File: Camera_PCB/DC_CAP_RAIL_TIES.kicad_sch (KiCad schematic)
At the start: 31 parts

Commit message: cleaned up Camera_PCB \repository
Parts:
- removed R11: 240, symbol Device:R
- added C75, C76, C77, C78, C79: 0.1u, Capacitor_SMD:C_0603_1608Metric_Pad1.08x0.95mm_HandSolder, symbol Device:C
- added R11: 240, Resistor_SMD:R_0603_1608Metric_Pad0.98x0.95mm_HandSolder, symbol Device:R_US
- added R30: 200k 1%, Resistor_SMD:R_0603_1608Metric_Pad0.98x0.95mm_HandSolder, symbol Device:R_Small_US
- C10: value 0.1u -> 1u; DPN (none) -> GCM188R71E105KA64D; Distributor (none) -> DigiKey; now not fitted
- C11, C12, C13, C14, C15, C16, C17, C18, C22, C23, C28, C29, C32, C33: DPN (none) -> GRM188R72A104KA35D; Distributor (none) -> DigiKey
- C19, C25, C30, C7: DPN (none) -> GRM21BZ71E106KE15L; Distributor (none) -> DigiKey
- C20, C26, C27, C31, C8, C9: footprint Capacitor_SMD:C_0805_2012Metric_Pad1.18x1.45mm_HandSolder -> Capacitor_SMD:C_0603_1608Metric_Pad1.08x0.95mm_HandSolder; DPN (none) -> GCM188R71E105KA64D; Distributor (none) -> DigiKey
- C21: footprint Capacitor_SMD:C_0805_2012Metric_Pad1.18x1.45mm_HandSolder -> Capacitor_SMD:C_0603_1608Metric_Pad1.08x0.95mm_HandSolder; DPN (none) -> GCM188R71E105KA64D; Distributor (none) -> DigiKey; now not fitted
- C24: DPN (none) -> GRM188R72A104KA35D; Distributor (none) -> DigiKey; now not fitted
- C37: DPN (none) -> GRM21BZ71H475ME15K; Distributor (none) -> DigiKey
- R10, R9: footprint Resistor_SMD:R_0805_2012Metric_Pad1.20x1.40mm_HandSolder -> Resistor_SMD:R_0603_1608Metric_Pad0.98x0.95mm_HandSolder; DPN (none) -> RC0603FR-102KL; Distributor (none) -> DigiKey
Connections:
- net +1V8: now also C75.2, C76.2
- net +3.3V: no longer C16.2
- net GND: now also C75.1, C76.1, C77.1, C78.1, C79.1, R11.2, R30.1
- net SVREF: now also C77.2
- net SZQ: now also R11.1
- new net VCC-RTC: C16.2
- new net VRA1: C79.2
- new net VRA2: C78.2, R30.2
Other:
- note added: "11 DRAM power pins, four physically separate groups of pins"
- note added: "Place close to v3s pin"
- note added: "Use +/-1% for these 2kR"
- note added: "Voltage Notes: 3.3V - VCC-IO, HPVCC, VCC-USB, VCC-EPHY, VCC-MCSI, VCC-PE 3.3V (always on) - VCC-RTC 3.0V - AVCC, VCC-PLL 1.8V - VCC-DRAM 1.2V - VDD-CPU, VDD-SYS UNPOWERED BUT DECOUPLED: VRA1, VRA2"
- note added: "use +/-1% R"
- note removed: "1.2V - VDD-CPU, VDD-SYS"
- note removed: "1.8V - VCC-DRAM"
- note removed: "3.0V - AVCC, VCC-PLL"
- note removed: "3.3V - VCC-IO, HPVCC, VCC-USB, VCC-EPHY, VCC-MCSI, VCC-PE, VCC-RTC"
- note removed: "Voltage Notes"
- moved on the sheet: C12, C13, C14, C15, C16, C17, C18, C19, C20, C22, C23, C37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

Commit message: Thorough Camera PCB Review by Jack
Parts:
- added TP14: SVREF, TestPoint:TestPoint_Pad_D1.5mm, symbol Connector:TestPoint
- added TP15: SZQ, TestPoint:TestPoint_Pad_D1.5mm, symbol Connector:TestPoint
- added TP28, TP29, TP30, TP31, TP32: GND, TestPoint:TestPoint_Pad_D1.5mm, symbol Connector:TestPoint
- R30: value 200k 1% -> 200k
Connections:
- net GND: now also TP28.1, TP29.1, TP30.1, TP31.1, TP32.1
- net SVREF: now also TP14.1
- net SZQ: now also TP15.1
- net +3.3V renamed +3V3
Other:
- note added: "Ground Test Points"
- note added: "Powered Decoupled Lines"
- note added: "Unpowered Decoupled Lines"
- moved on the sheet: C18, C78, R30

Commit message: more schematic changes, added solder bridges, etc
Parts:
- TP14, TP15, TP28, TP29, TP30, TP31, TP32: now left out of the parts list
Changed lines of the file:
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@@
 		(unit 1)
 		(exclude_from_sim no)
-		(in_bom yes)
+		(in_bom no)
 		(on_board yes)
 		(dnp no)
@@
 		(unit 1)
 		(exclude_from_sim no)
-		(in_bom yes)
+		(in_bom no)
 		(on_board yes)
 		(dnp no)
@@
 		(unit 1)
 		(exclude_from_sim no)
-		(in_bom yes)
+		(in_bom no)
 		(on_board yes)
 		(dnp no)
@@
 		(unit 1)
 		(exclude_from_sim no)
-		(in_bom yes)
+		(in_bom no)
 		(on_board yes)
 		(dnp no)
@@
 		(unit 1)
 		(exclude_from_sim no)
-		(in_bom yes)
+		(in_bom no)
 		(on_board yes)
 		(dnp no)
@@
 		(unit 1)
 		(exclude_from_sim no)
-		(in_bom yes)
+		(in_bom no)
 		(on_board yes)
 		(dnp no)
@@
 		(unit 1)
 		(exclude_from_sim no)
-		(in_bom yes)
+		(in_bom no)
 		(on_board yes)
 		(dnp no)

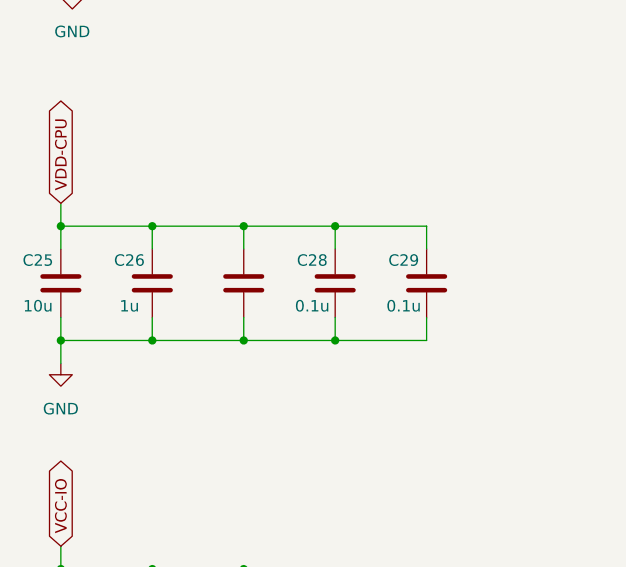
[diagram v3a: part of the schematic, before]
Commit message: PCB commit before reorganizing
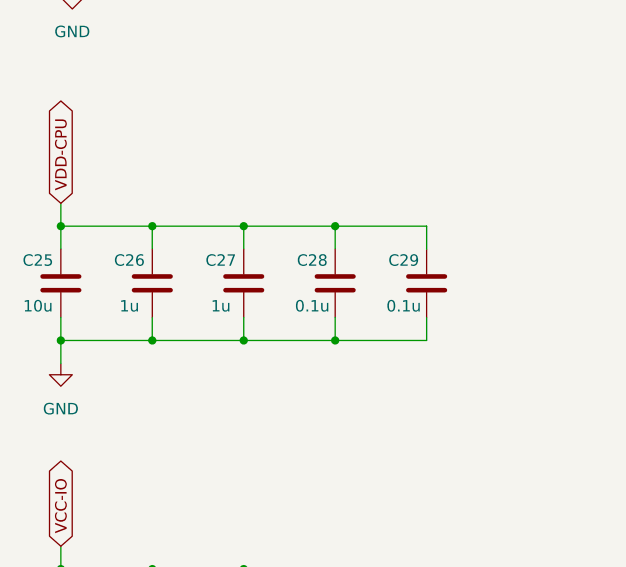
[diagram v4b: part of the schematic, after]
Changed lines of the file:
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@@
 					(size 1.27 1.27)
 				)
-				(hide yes)
 			)
 		)
@@
 					(size 1.27 1.27)
 				)
-				(hide yes)
 			)
 		)

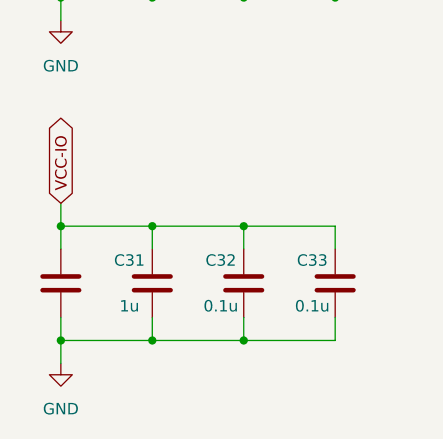
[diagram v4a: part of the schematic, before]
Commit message: Shrunk camera PCB and rearranged connectors. Everything on board. Not everything connected.
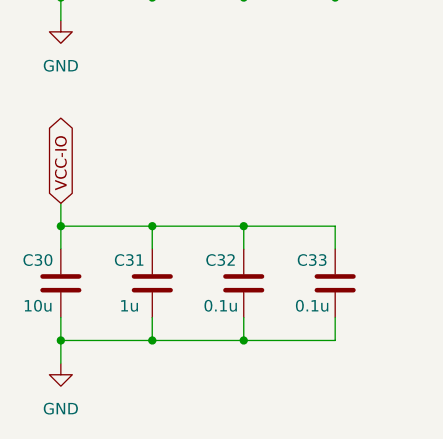
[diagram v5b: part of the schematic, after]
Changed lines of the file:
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@@
 					(size 1.27 1.27)
 				)
-				(hide yes)
 			)
 		)
@@
 					(size 1.27 1.27)
 				)
-				(hide yes)
 			)
 		)
